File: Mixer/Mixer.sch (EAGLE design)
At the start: 43 parts, among them IC1 LM741P, IC2 LM741P, T1 2N3904

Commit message: Created Board File
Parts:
- added MASTER_OUT: (no value), pinhead:PINHD-1X2
- added POWER: 1-770875-0, Capstone:1-770875-0
- renumbered JP1 to TO_POTS, JP2 to INSTRUMENTS_IN, JP3 to VU_METER
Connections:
- removed net N$29: TO_POTS.27
- removed net N$30: TO_POTS.29
- removed net N$31: TO_POTS.31
- removed net N$32: TO_POTS.33
- removed net N$33: TO_POTS.35
- removed net N$34: TO_POTS.37
- removed net N$49: TO_POTS.28
- removed net N$50: TO_POTS.30
- removed net N$51: TO_POTS.32
- removed net N$52: TO_POTS.34
- removed net N$53: TO_POTS.36
- removed net N$54: TO_POTS.38
- removed net N$55: TO_POTS.40
- new net +5V: POWER.6, TO_POTS.37
- net +12V: now also POWER.4, TO_POTS.33
- net -12V: now also POWER.5, TO_POTS.35
- net GND: now also MASTER_OUT.2, POWER.1, POWER.2, POWER.3, TO_POTS.12, TO_POTS.18, TO_POTS.24, TO_POTS.27, TO_POTS.29, TO_POTS.30, TO_POTS.31, TO_POTS.36, TO_POTS.40, TO_POTS.6; no longer INSTRUMENTS_IN.8
- net INST10_OUT: now also TO_POTS.32; no longer TO_POTS.22
- net INST11_OUT: now also TO_POTS.34; no longer TO_POTS.24
- net INST12_OUT: now also TO_POTS.38; no longer TO_POTS.26
- net INST2_OUT: now also TO_POTS.8; no longer TO_POTS.6
- net INST3_OUT: now also TO_POTS.10; no longer TO_POTS.8
- net INST4_OUT: now also TO_POTS.14; no longer TO_POTS.10
- net INST5_OUT: now also TO_POTS.16; no longer TO_POTS.12
- net INST6_OUT: now also TO_POTS.20; no longer TO_POTS.14
- net INST7_OUT: now also TO_POTS.22; no longer TO_POTS.16
- net INST8_OUT: now also TO_POTS.26; no longer TO_POTS.18
- net INST9_OUT: now also TO_POTS.28; no longer TO_POTS.20
- net SIG_OUT: now also MASTER_OUT.1
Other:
- note added: "Andrew Schroeder"
- note added: "REV 1.0"

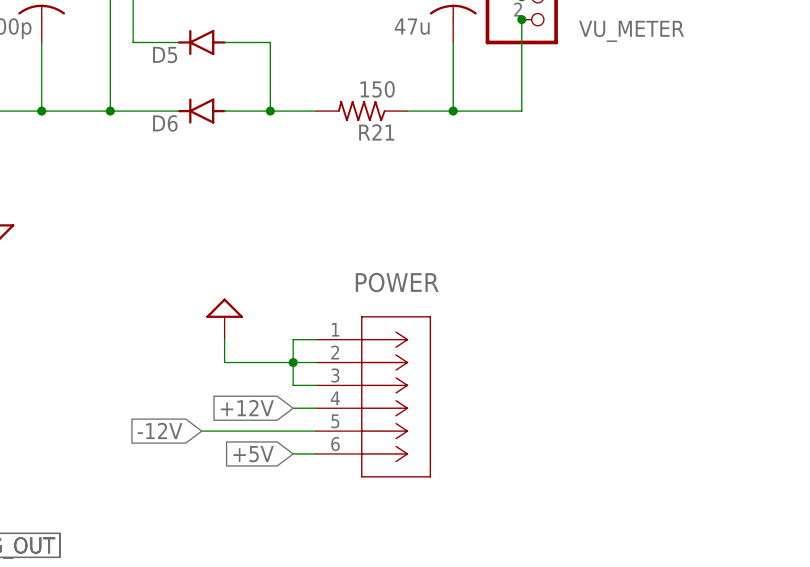
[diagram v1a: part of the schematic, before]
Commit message: Completed Mixer Board Layout
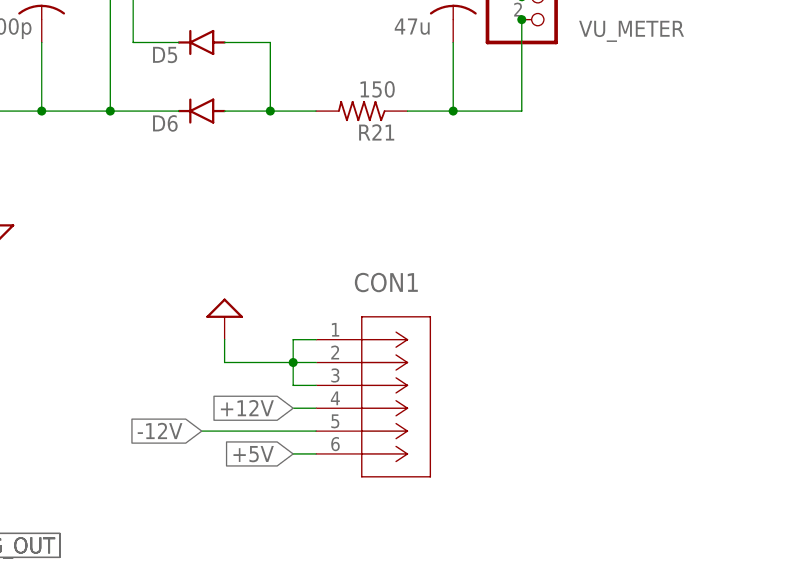
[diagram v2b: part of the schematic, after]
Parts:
- removed POWER: 1-770875-0, Capstone:1-770875-0
- added CON1: 1-770875-01-770875-0_VERTICAL, Capstone:1-770875-01-770875-0_VERTICAL
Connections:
- net +12V: now also CON1.4; no longer POWER.4
- net +5V: now also CON1.6; no longer POWER.6
- net -12V: now also CON1.5; no longer POWER.5
- net GND: now also CON1.1, CON1.2, CON1.3; no longer POWER.1, POWER.2, POWER.3
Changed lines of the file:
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@@
 <part name="MASTER_OUT" library="pinhead" library_urn="urn:adsk.eagle:library:325" deviceset="PINHD-1X2" device="" package3d_urn="urn:adsk.eagle:package:22435/2"/>
 <part name="GND14" library="audio amplifier example" library_urn="urn:adsk.eagle:library:970892" deviceset="GND" device="" value="SUP"/>
-<part name="POWER" library="Capstone" deviceset="1-770875-0" device=""/>
+<part name="CON1" library="Capstone" deviceset="1-770875-0" device="1-770875-0_VERTICAL"/>
 </parts>
 <sheets>
@@
 </instance>
 <instance part="GND14" gate="G$1" x="182.88" y="22.86" smashed="yes" rot="MR0"/>
-<instance part="POWER" gate="A" x="215.9" y="60.96" smashed="yes">
+<instance part="CON1" gate="A" x="215.9" y="60.96" smashed="yes">
 <attribute name="NAME" x="220.0656" y="66.2686" size="2.0828" layer="95" ratio="6" rot="SR0"/>
 </instance>
@@
 <wire x1="215.9" y1="50.8" x2="203.2" y2="50.8" width="0.1524" layer="91"/>
 <label x="203.2" y="50.8" size="1.778" layer="95" rot="R180" xref="yes"/>
-<pinref part="POWER" gate="A" pin="5"/>
+<pinref part="CON1" gate="A" pin="5"/>
 </segment>
 <segment>
@@
 <wire x1="205.74" y1="58.42" x2="205.74" y2="60.96" width="0.1524" layer="91"/>
 <pinref part="GND13" gate="G$1" pin="GND"/>
-<pinref part="POWER" gate="A" pin="1"/>
-<pinref part="POWER" gate="A" pin="2"/>
-<pinref part="POWER" gate="A" pin="3"/>
+<pinref part="CON1" gate="A" pin="1"/>
+<pinref part="CON1" gate="A" pin="2"/>
+<pinref part="CON1" gate="A" pin="3"/>
 </segment>
 <segment>
@@
 <wire x1="215.9" y1="53.34" x2="213.36" y2="53.34" width="0.1524" layer="91"/>
 <label x="213.36" y="53.34" size="1.778" layer="95" rot="R180" xref="yes"/>
-<pinref part="POWER" gate="A" pin="4"/>
+<pinref part="CON1" gate="A" pin="4"/>
 </segment>
 <segment>
@@
 <wire x1="215.9" y1="48.26" x2="213.36" y2="48.26" width="0.1524" layer="91"/>
 <label x="213.36" y="48.26" size="1.778" layer="95" rot="R180" xref="yes"/>
-<pinref part="POWER" gate="A" pin="6"/>
-</segment>
-<segment>
+<pinref part="CON1" gate="A" pin="6"/>
+</segment>
+<segment>
